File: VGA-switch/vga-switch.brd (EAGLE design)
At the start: 64.4 x 63.5 mm, 17 parts, among them J1 2.1MMJACKTHM, K1 RR2A, K2 RR2A, K3 RR2A, K4 RR2A, K5 RR2A, K6 RR2A, K7 RR2A, K8 RR2A, X1 D-SUB15-HDR15RA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

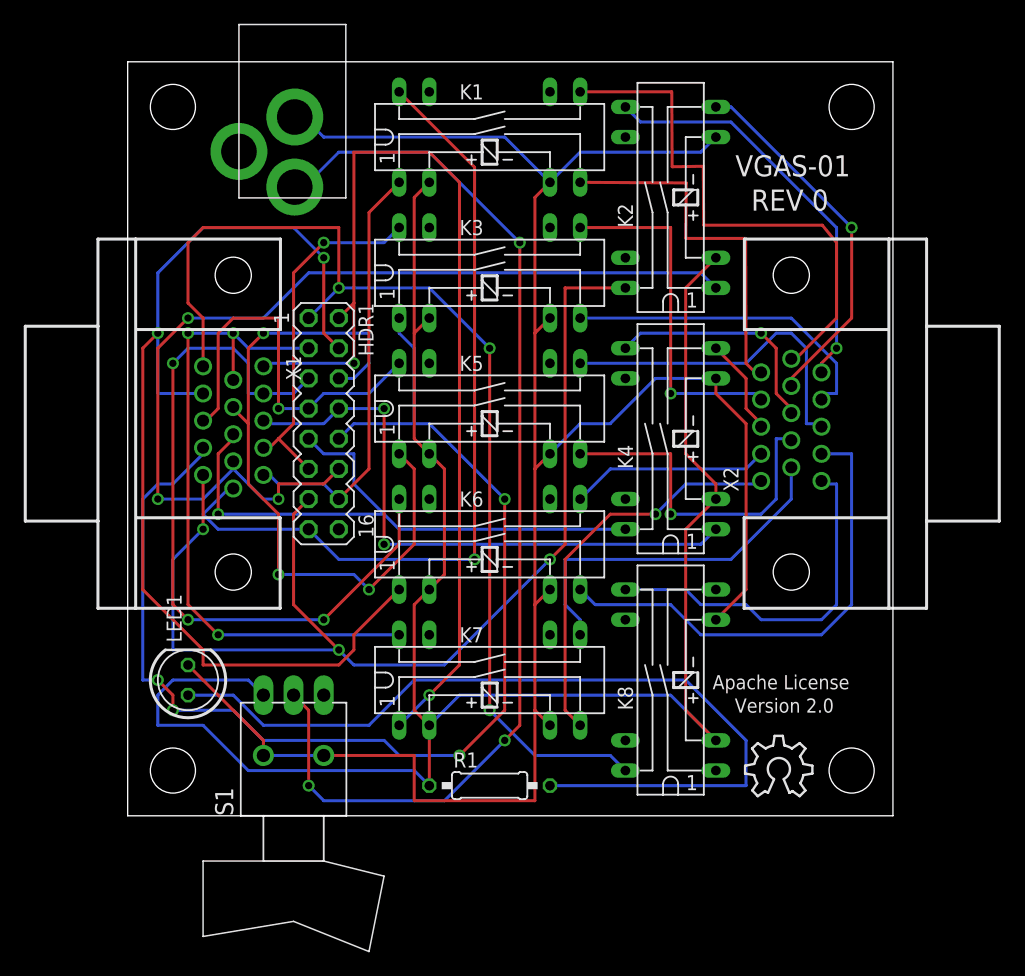
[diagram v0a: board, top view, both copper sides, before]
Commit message: Revision to rev 2
Changes for rev 2:

There was a via under the power switch which could short to the switch frame.
This has been moved, and an exclusion zone has been added on the top layer where the switch frame is.

Added URL to the silkscreen

Changed rev number on silkscreen
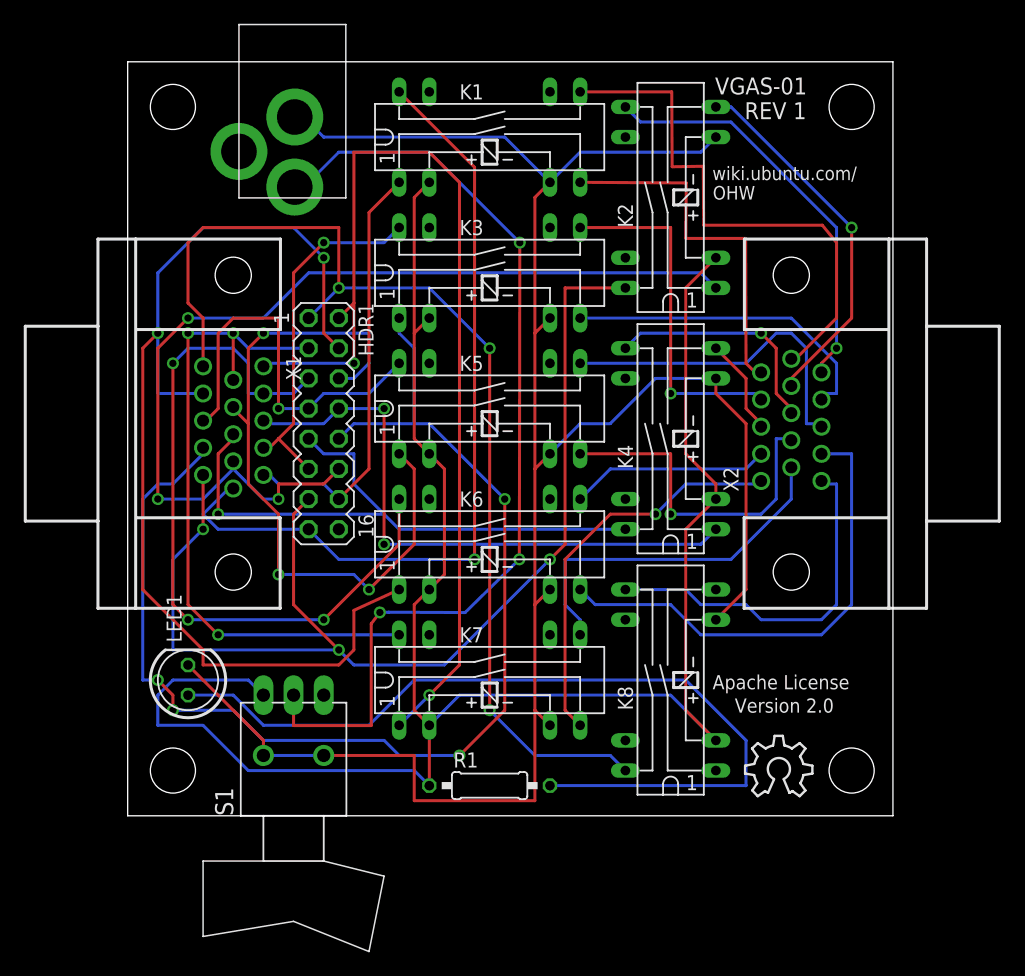
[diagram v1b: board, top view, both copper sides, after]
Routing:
- net N$1: track 92.9 -> 82.3 mm
- net N$16: track 89.2 -> 90.0 mm
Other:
- board text added: "OHW"
- board text added: "REV 1"
- board text added: "wiki.ubuntu.com/"
- board text removed: "REV 0"
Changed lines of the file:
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@@
 <layer number="39" name="tKeepout" color="4" fill="11" visible="no" active="yes"/>
 <layer number="40" name="bKeepout" color="1" fill="11" visible="no" active="yes"/>
-<layer number="41" name="tRestrict" color="4" fill="10" visible="no" active="yes"/>
+<layer number="41" name="tRestrict" color="4" fill="10" visible="yes" active="yes"/>
 <layer number="42" name="bRestrict" color="1" fill="10" visible="no" active="yes"/>
 <layer number="43" name="vRestrict" color="2" fill="10" visible="no" active="yes"/>
@@
 <rectangle x1="0.7475" y1="0.1775" x2="0.7955" y2="0.1785" layer="200"/>
 <rectangle x1="-0.0005" y1="0.1785" x2="0.7955" y2="0.1795" layer="200"/>
-<text x="51.167" y="53.843" size="1.778" layer="121">VGAS-01</text>
-<text x="52.505" y="50.955" size="1.778" layer="121">REV 0</text>
 <text x="49.25065" y="10.6529125" size="1.1938" layer="25">Apache License</text>
 <text x="51.1199125" y="8.684590625" size="1.1938" layer="25">Version 2.0</text>
+<rectangle x1="9.50084375" y1="0" x2="18.434075" y2="3.97626875" layer="41"/>
+<text x="49.45570625" y="60.743590625" size="1.4224" layer="121">VGAS-01</text>
+<text x="51.9470625" y="58.66135" size="1.4224" layer="121">REV 1</text>
+<text x="49.231828125" y="53.527071875" size="1.143" layer="121">wiki.ubuntu.com/</text>
+<text x="49.26848125" y="51.8906" size="1.143" layer="121">OHW</text>
 </plain>
 <attributes>
@@
 <contactref element="J1" pad="TIP"/>
 <contactref element="S1" pad="2"/>
-<wire x1="15.24" y1="8.89" x2="13.97" y2="10.16" width="0.254" layer="1"/>
-<wire x1="15.24" y1="2.54" x2="15.24" y2="8.89" width="0.254" layer="1"/>
-<wire x1="16.51" y1="1.27" x2="15.24" y2="2.54" width="0.254" layer="16"/>
-<wire x1="26.67" y1="1.27" x2="16.51" y2="1.27" width="0.254" layer="16"/>
-<wire x1="31.75" y1="6.35" x2="26.67" y2="1.27" width="0.254" layer="16"/>
-<wire x1="33.02" y1="7.62" x2="31.75" y2="6.35" width="0.254" layer="1"/>
-<wire x1="33.02" y1="48.26" x2="33.02" y2="7.62" width="0.254" layer="1"/>
+<wire x1="13.967078125" y1="7.599246875" x2="13.97" y2="10.16" width="0.254" layer="1"/>
+<wire x1="21.234121875" y1="17.1246" x2="20.5074" y2="16.1695625" width="0.254" layer="1"/>
+<wire x1="20.5074" y1="16.1695625" x2="20.5074" y2="7.599246875" width="0.254" layer="1"/>
+<wire x1="20.5074" y1="7.599246875" x2="13.967078125" y2="7.599246875" width="0.254" layer="1"/>
+<wire x1="21.984334375" y1="17.14299375" x2="21.234121875" y2="17.1246" width="0.254" layer="16"/>
+<wire x1="28.41048125" y1="17.11365625" x2="21.984334375" y2="17.14299375" width="0.254" layer="16"/>
+<wire x1="32.97735" y1="21.593353125" x2="28.41048125" y2="17.11365625" width="0.254" layer="16"/>
+<wire x1="32.992259375" y1="27.70243125" x2="32.97735" y2="21.593353125" width="0.254" layer="1"/>
+<wire x1="33.02" y1="48.26" x2="32.992259375" y2="27.70243125" width="0.254" layer="1"/>
 <wire x1="25.4" y1="55.88" x2="33.02" y2="48.26" width="0.254" layer="16"/>
 <wire x1="17.78" y1="55.88" x2="25.4" y2="55.88" width="0.254" layer="16"/>
 <wire x1="15.24" y1="53.34" x2="17.78" y2="55.88" width="0.254" layer="16"/>
 <wire x1="15.24" y1="53.34" x2="14.07" y2="52.94" width="0.254" layer="16"/>
-<via x="15.24" y="2.54" extent="1-16" drill="0.6096"/>
-<via x="31.75" y="6.35" extent="1-16" drill="0.6096"/>
+<via x="21.234121875" y="17.1246" extent="1-16" drill="0.6096"/>
+<via x="32.97735" y="21.593353125" extent="1-16" drill="0.6096"/>
 <via x="33.02" y="48.26" extent="1-16" drill="0.6096"/>
 </signal>
@@
 <contactref element="K6" pad="1"/>
 <contactref element="HDR1" pad="4"/>
-<wire x1="19.05" y1="15.24" x2="22.86" y2="19.05" width="0.254" layer="1"/>
-<wire x1="19.05" y1="13.97" x2="19.05" y2="15.24" width="0.254" layer="1"/>
+<wire x1="19.049009375" y1="17.30045" x2="22.86" y2="19.05" width="0.254" layer="1"/>
+<wire x1="19.05" y1="13.97" x2="19.049009375" y2="17.30045" width="0.254" layer="1"/>
 <wire x1="17.78" y1="12.7" x2="19.05" y2="13.97" width="0.254" layer="1"/>
 <wire x1="6.35" y1="12.7" x2="17.78" y2="12.7" width="0.254" layer="1"/>
